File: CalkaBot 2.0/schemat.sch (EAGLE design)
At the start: 48 parts, among them IC1 TB6612FNG, IC2 LM339D, IC3 7806DT, Q1 16MHz, X1 MINI-USB-32005-301

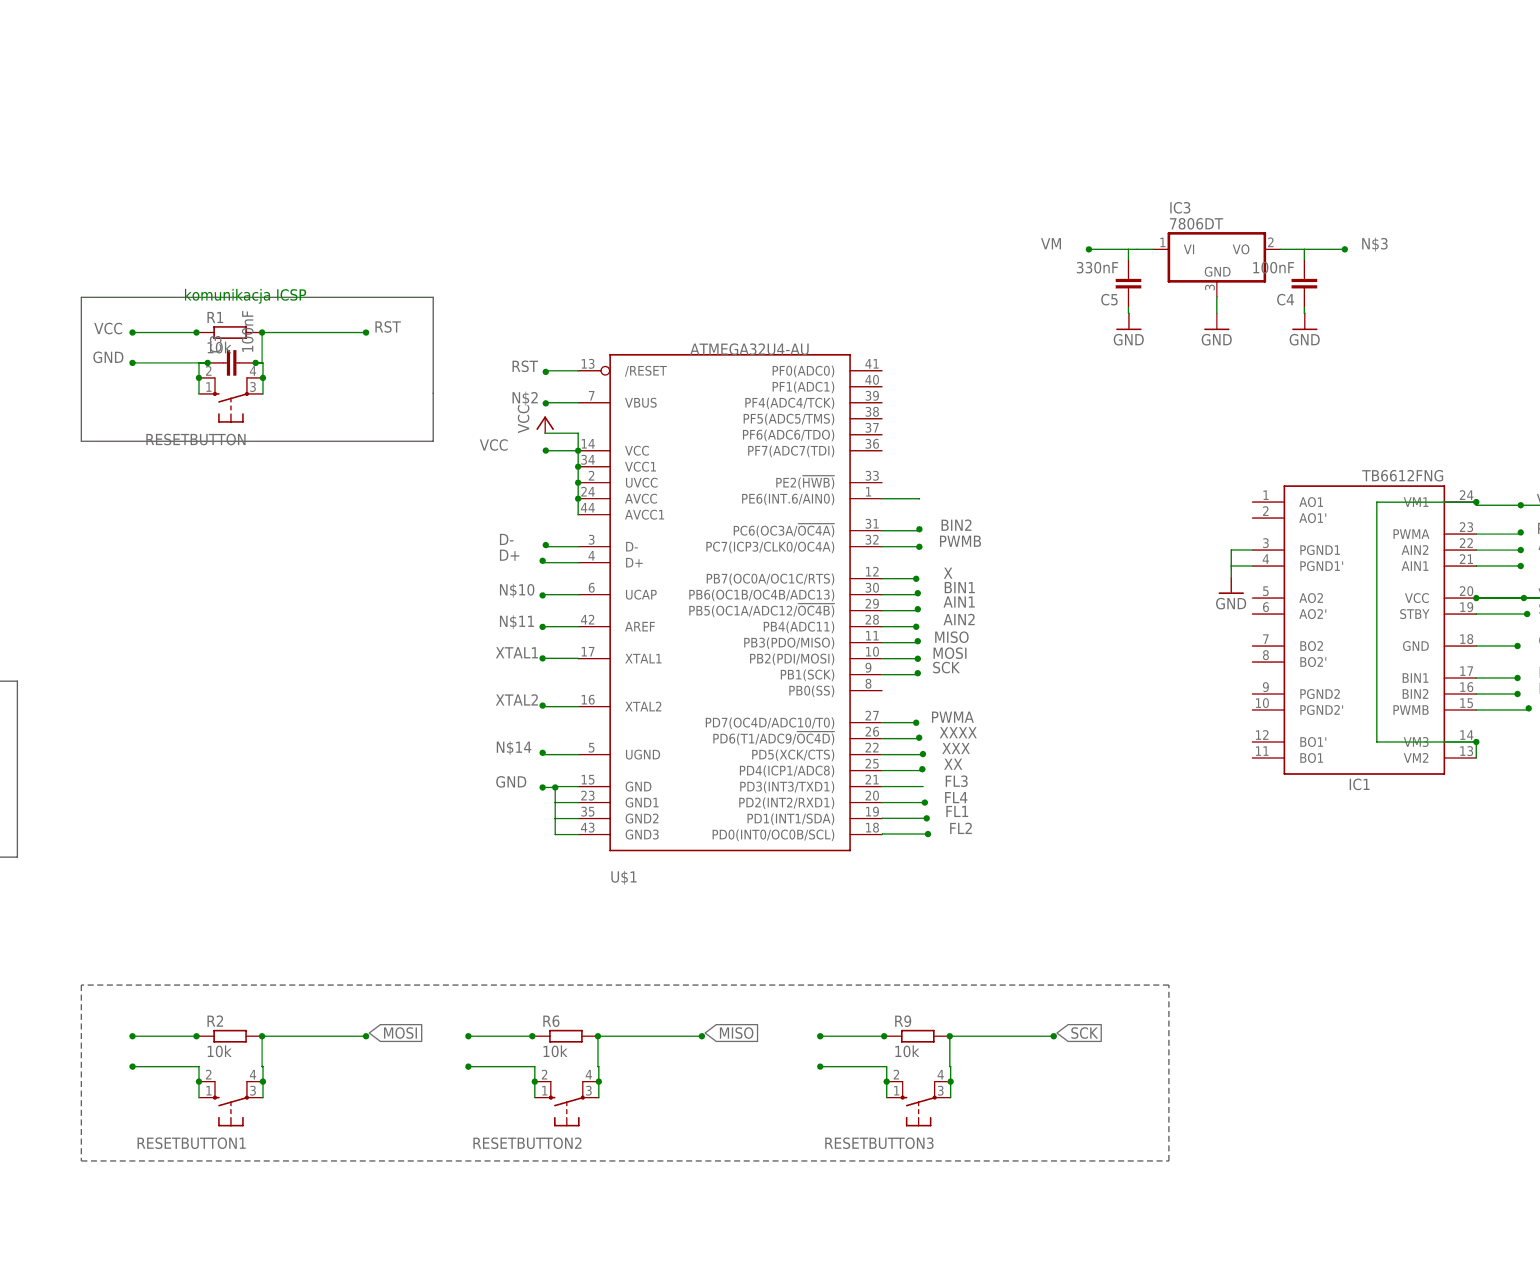
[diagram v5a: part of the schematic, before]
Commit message: podłączenie przycisków teraz
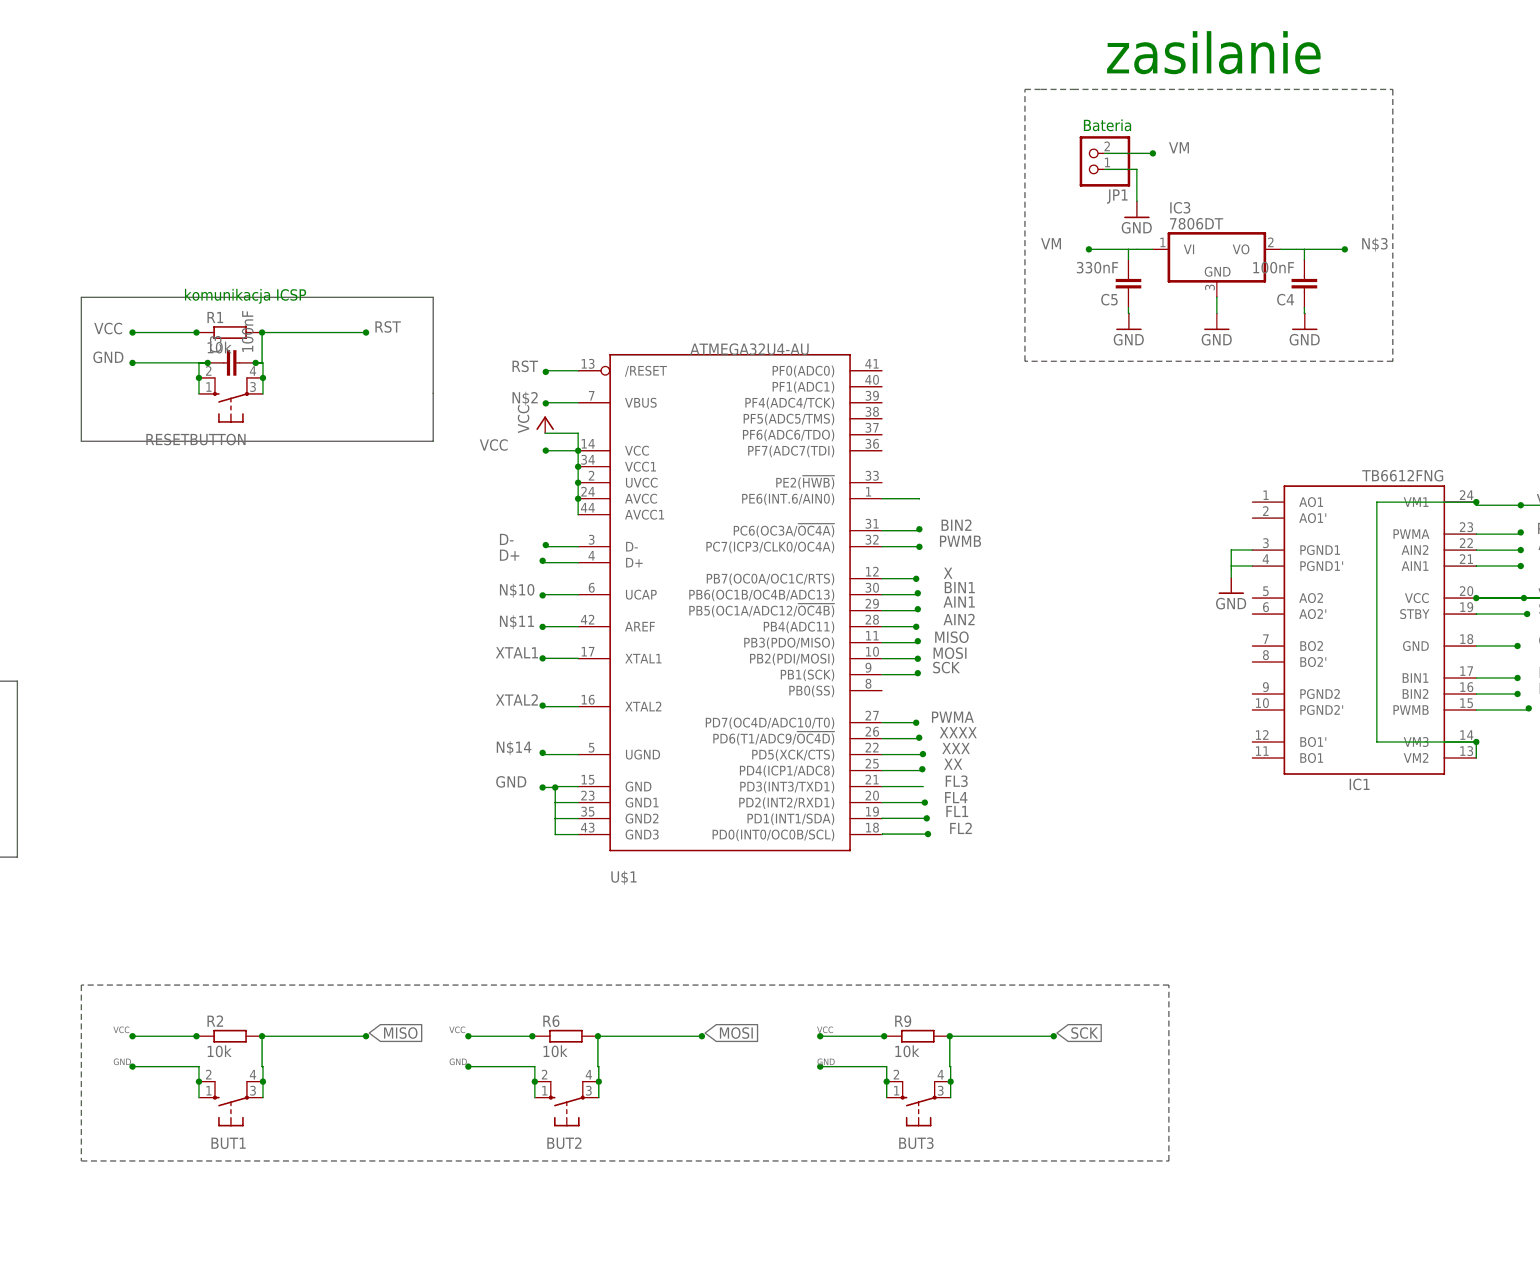
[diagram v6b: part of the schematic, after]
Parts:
- added JP1: (no value), pinhead:PINHD-1X2
- renumbered RESETBUTTON1 to BUT1, RESETBUTTON2 to BUT2, RESETBUTTON3 to BUT3
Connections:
- removed net GND2: BUT2.S, BUT2.S1
- removed net GND3: BUT3.S, BUT3.S1
- removed net VCC2: R6.1
- removed net VCC3: R9.1
- net GND: now also BUT2.S, BUT2.S1, BUT3.S, BUT3.S1, JP1.1
- net MISO: now also BUT1.P, BUT1.P1, R2.2; no longer BUT2.P, BUT2.P1, R6.2
- net MOSI: now also BUT2.P, BUT2.P1, R6.2; no longer BUT1.P, BUT1.P1, R2.2
- net VCC: now also R6.1, R9.1
- net VM: now also JP1.2
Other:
- note added: "Bateria"
- note added: "zasilanie"

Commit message: nie ma miejsca na usb, pcb prawie skończone
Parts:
- removed U$3, U$4, U$5, U$6: CNY70, cny70:CNY70
- added C10: 1uF, rcl:CPOL-USUD-4X5,8
- added JP2, JP3: (no value), pinhead:PINHD-1X5
- added LED5, LED6: (no value), led:LEDCHIP-LED0805
- added R12, R22: 220R, rcl:R-EU_R0805
- added R25, R26: 22R, rcl:R-EU_R0805
- added SW1: (no value), special:SW_DIP-1
- RESETBUTTON: value (none) -> DTS-3; device switch-omron:10-XX -> switch-tact (1):DTS-3
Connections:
- net N$8 renamed I/O11
- net X renamed I/O12
- net XX renamed I/O9
- net XXX renamed I/O8
- net XXXX renamed I/O7
- removed net ID: X1.2
- removed net N$10: U$1.UCAP
- removed net N$11: U$1.AREF
- removed net N$14: U$1.UGND
- removed net N$2: U$1.VBUS
- removed net N$3: C4.2, IC3.VO
- new net AO1: IC1.AO1, IC1.AO1'
- new net AO2: IC1.AO2, IC1.AO2'
- new net BO1: IC1.BO1, IC1.BO1'
- new net BO2: IC1.BO2, IC1.BO2'
- new net I/O1: U$1.PF0(ADC0)
- new net I/O10: U$1.PE2(!HWB)
- new net I/O2: U$1.PF1(ADC1)
- new net I/O3: U$1.PF4(ADC4/TCK)
- new net I/O4: U$1.PF5(ADC5/TMS)
- new net I/O5: U$1.PF6(ADC6/TDO)
- new net I/O6: U$1.PF7(ADC7(TDI)
- new net N$12: JP2.3, JP3.3, R25.1, X1.3
- new net N$20: JP2.4, JP3.4, R26.1, X1.4
- new net N$7: LED5.A, R12.1
- new net N$9: LED6.A, R22.1
- new net PIN: JP1.2, SW1.1
- new net UCAP: C10.+, U$1.UCAP
- new net VBUS: JP2.5, JP3.5, U$1.VBUS, X1.5
- net D+: now also R25.2; no longer X1.3
- net D-: now also R26.2; no longer X1.4
- net GND: now also C10.-, IC1.PGND1, IC1.PGND1', IC1.PGND2, IC1.PGND2', JP2.1, JP2.2, JP3.1, JP3.2, LED5.C, LED6.C, RESETBUTTON.2, U$1.UGND, X1.2; no longer RESETBUTTON.S, RESETBUTTON.S1, U$3.C, U$3.EMI, U$4.C, U$4.EMI, U$5.C, U$5.EMI, U$6.C, U$6.EMI
- net N$1: no longer U$3.A
- net N$19: no longer U$4.A
- net N$23: no longer U$5.A
- net N$27: no longer U$6.A
- net RST: now also RESETBUTTON.1; no longer RESETBUTTON.P, RESETBUTTON.P1
- net S1: no longer U$3.COL
- net S2: no longer U$4.COL
- net S3: no longer U$5.COL
- net S4: no longer U$6.COL
- net VCC: now also C4.2, IC3.VO, R12.2, U$1.AREF; no longer X1.5
- net VM: now also R22.2, SW1.2; no longer JP1.2
